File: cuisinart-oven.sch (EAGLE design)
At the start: 43 parts, among them CN1 CN1, CON1 CON1, IC3 P1014AP06, IC4 PC817, K1 V23148-A0003-B101-NO, K2 V23148-A0003-B101-NO, T1 TICP206, T2 BD705

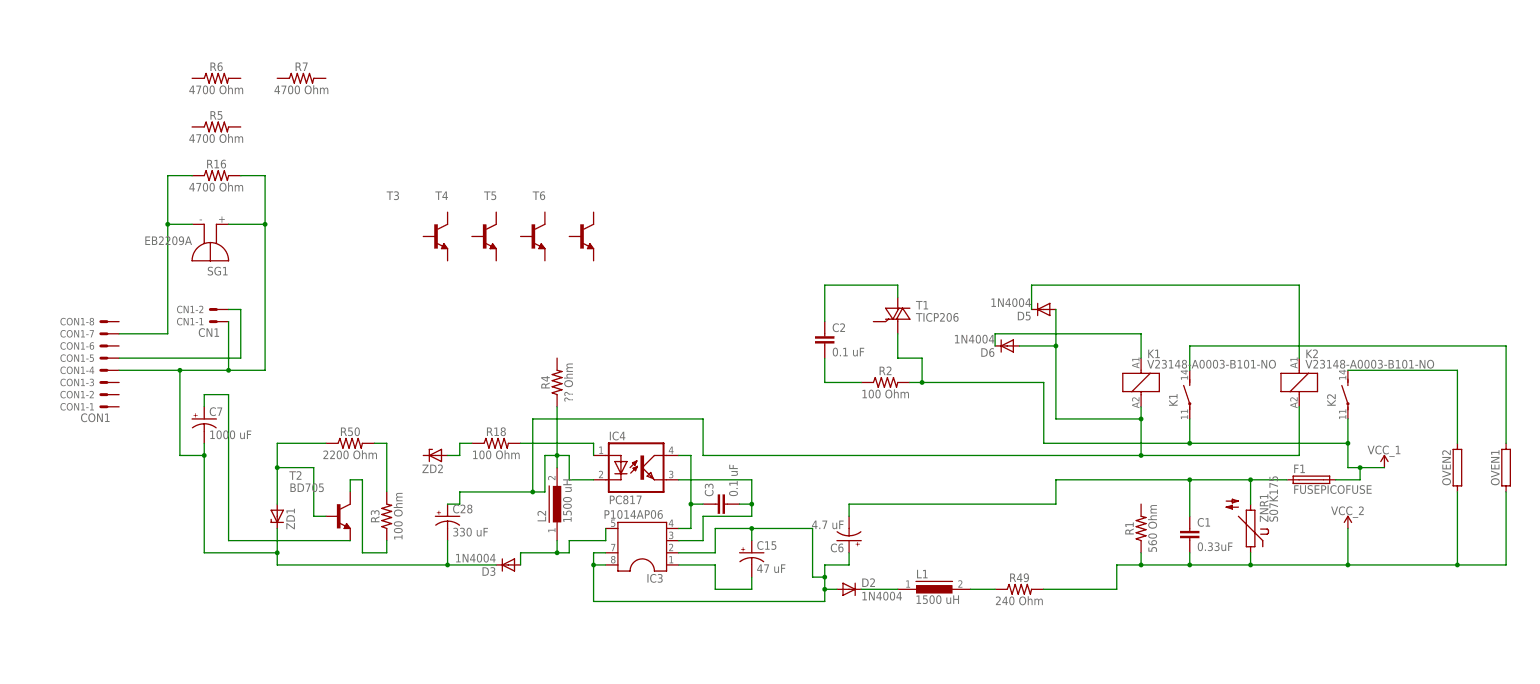
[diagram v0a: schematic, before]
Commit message: Complete schematic
Finally the circuit is complete.
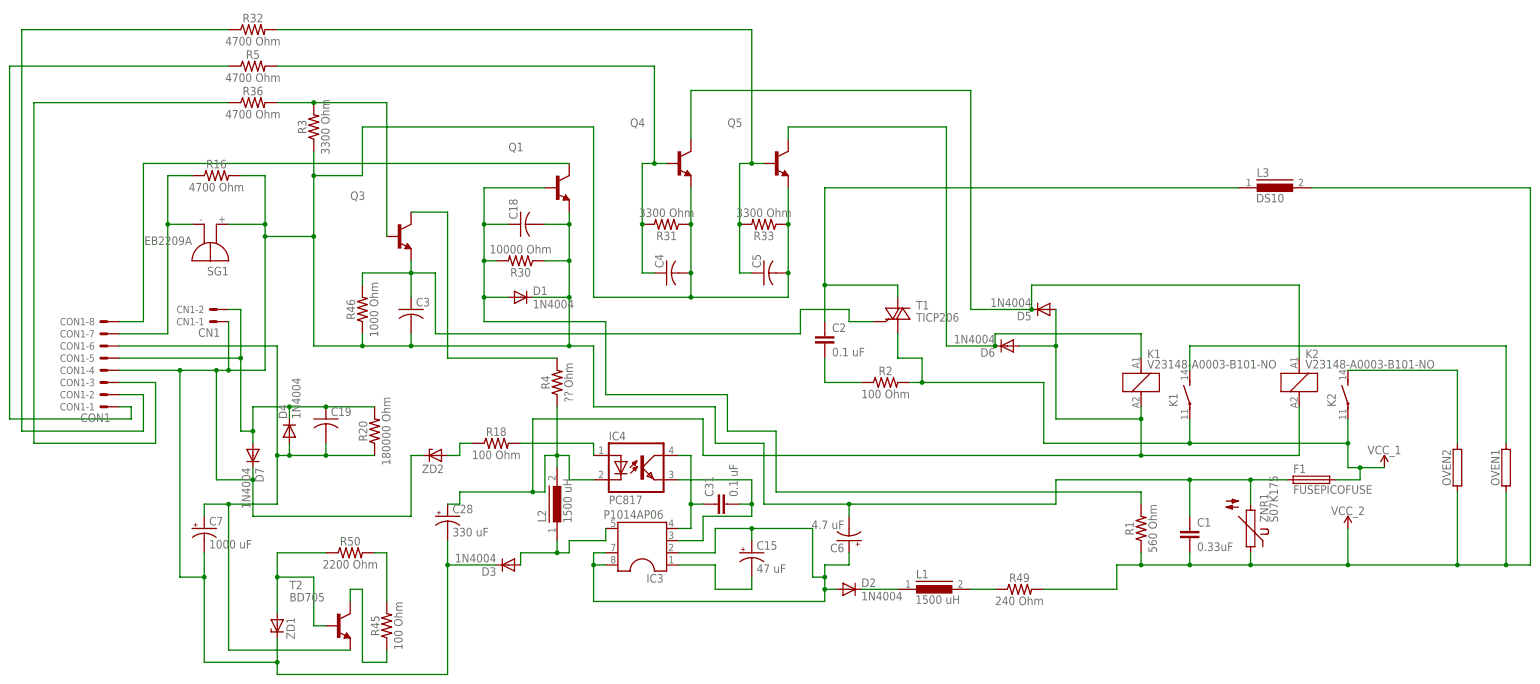
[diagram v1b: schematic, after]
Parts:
- removed R6, R7: 4700 Ohm, SparkFun-Resistors:RESISTORAXIAL-0.3
- removed T3, T4, T5, T6: (no value), transistor:BFS17-NPN-SOT23-BEC
- added C18, C19, C4, C5: (no value), rcl:C-US025-024X044
- added C31: 0.1 uF, rcl:CXXC15B6
- added D1, D4, D7: 1N4004, diode:1N4004
- added L3: DS10, inductors:DS10
- added Q1, Q3, Q4, Q5: (no value), transistor:BFS17-NPN-SOT23-BEC
- added R20: 180000 Ohm, SparkFun-Resistors:RESISTORAXIAL-0.3
- added R30: 10000 Ohm, SparkFun-Resistors:RESISTORAXIAL-0.3
- added R31, R33: 3300 Ohm, SparkFun-Resistors:RESISTORAXIAL-0.3
- added R32, R36: 4700 Ohm, SparkFun-Resistors:RESISTORAXIAL-0.3
- added R45: 100 Ohm, SparkFun-Resistors:RESISTORAXIAL-0.3
- added R46: 1000 Ohm, SparkFun-Resistors:RESISTORAXIAL-0.3
- C3: value 0.1 uF -> (none); device rcl:CXXC15B6 -> rcl:C-US025-024X044
- R3: value 100 Ohm -> 3300 Ohm
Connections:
- removed net N$24: C7.+, T2.E
- new net N$10: CON1-3.S, R36.1
- new net N$26: Q3.B, R3.2, R36.2
- new net N$27: Q3.C, R4.2
- new net N$28: C3.1, Q3.E, R46.2, T1.G
- new net N$29: CON1-8.S, Q1.C
- new net N$30: C5.1, Q5.B, R32.2, R33.2
- new net N$31: C19.2, C7.+, CON1-6.S, D4.A, R20.1, T2.E
- new net N$33: C4.1, Q4.B, R31.2, R5.2
- new net N$34: CON1-2.S, R32.1
- new net N$37: CON1-1.S, R5.1
- net N$12: now also L3.1
- net N$13: now also C31.2; no longer C3.2
- net N$14: now also C18.2, C28.-, C3.2, C4.2, C5.2, C7.-, CN1-1.S, CON1-4.S, D1.C, D3.C, D7.C, Q1.E, Q4.E, Q5.E, R16.2, R3.1, R30.1, R31.1, R33.1, R46.1, SG1.+, ZD1.CATHODE, ZD2.CATHODE
- net N$15: now also C31.1; no longer C3.1
- net N$19: now also C18.1, D1.A, Q1.B, R1.2, R30.2; no longer C28.-, C7.-, CN1-1.S, CON1-4.S, D3.C, R16.2, SG1.+, ZD1.CATHODE
- net N$21: now also R45.1; no longer R3.1
- net N$22: now also R45.2; no longer R3.2
- net N$25: now also C19.1, D4.C, D7.A, R20.2
- net N$6: now also Q4.C
- net N$8: now also Q5.C
- net VCC_2: now also L3.2
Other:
- moved on the sheet: C3, C7, R3, R5, R50, T2, ZD1
